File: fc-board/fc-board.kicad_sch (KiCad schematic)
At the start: 11 parts, among them J1 ESQ-125-14-G-D, J2 MSXS-08PFFR-SF7002, J8 M80-5000442

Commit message: Fc board (#9)
* FC board updates

* Finished routing; cleaned library

* Updated RJ45 jack

* Assigned part numbers to everything, replaced ethernet jack

* Finalized layout

* V1 sent for printing
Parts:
- removed J1: ESQ-125-14-G-D, fc-board:ESQ-125-XX-X-D, symbol fc-board:ESQ-125-XX-X-D
- removed J2: MSXS-08PFFR-SF7002, fc-board:MSXS-08PFFR-SF7002, symbol fc-board:MSXS-08PFFR-SF7002
- removed JP14: P1 to GND, Jumper:SolderJumper-2_P1.3mm_Open_Pad1.0x1.5mm, symbol Jumper:SolderJumper_2_Open
- added J1, J3, J4, J5: M80-5000442, fc-board:M80_5000442, symbol fc-board:M80-5000442
- added J10: MTSW-110-13-L-D-1060, fc-board:SAMTEC_BCS-110-L-D-TE, symbol Connector_Generic:Conn_02x10_Odd_Even
- added J11: Conn_Coaxial_Small, Connector_Coaxial:MMCX_Molex_73415-1471_Vertical, symbol Connector:Conn_Coaxial_Small
- added J12: Conn_01x03_Pin, Connector_PinHeader_2.54mm:PinHeader_1x03_P2.54mm_Vertical, symbol Connector:Conn_01x03_Pin
- added J13: 74981104402, fc-board:74981104402, symbol fc-board:74981104402
- added J6: MTSW-104-13-L-D-1060, Connector_PinSocket_2.54mm:PinSocket_2x04_P2.54mm_Vertical, symbol Connector_Generic:Conn_02x04_Counter_Clockwise
- added J7: Conn_02x02_Counter_Clockwise, Connector_PinHeader_2.54mm:PinHeader_2x02_P2.54mm_Vertical, symbol Connector_Generic:Conn_02x02_Counter_Clockwise
- added J8: Conn_01x08_Pin, Connector_PinHeader_2.54mm:PinHeader_2x04_P2.54mm_Vertical, symbol Connector:Conn_01x08_Pin
- added J9: Conn_01x02_Pin, Connector_PinHeader_2.54mm:PinHeader_1x02_P2.54mm_Vertical, symbol Connector:Conn_01x02_Pin
- added JP1: nRPIBOOT, Jumper:SolderJumper-2_P1.3mm_Open_Pad1.0x1.5mm, symbol Jumper:SolderJumper_2_Open
- added JP2: CHASSIS_GND, Jumper:SolderJumper-2_P1.3mm_Open_Pad1.0x1.5mm, symbol Jumper:SolderJumper_2_Open
- added R2, R3: 330, Resistor_SMD:R_1206_3216Metric, symbol Device:R_Small
- added TP1: SDA0, fc-board:TestPoint_THTPad_D2.0mm_Drill1.0mm_JLCrules, symbol Connector:TestPoint
- added TP10: Global_EN, fc-board:TestPoint_THTPad_D2.0mm_Drill1.0mm_JLCrules, symbol Connector:TestPoint
- added TP2: SCL0, fc-board:TestPoint_THTPad_D2.0mm_Drill1.0mm_JLCrules, symbol Connector:TestPoint
- added TP5: +5V, fc-board:TestPoint_THTPad_D2.0mm_Drill1.0mm_JLCrules, symbol Connector:TestPoint
- added TP6: ADS_DRDY, fc-board:TestPoint_THTPad_D2.0mm_Drill1.0mm_JLCrules, symbol Connector:TestPoint
- added TP7: nEXTRST, fc-board:TestPoint_THTPad_D2.0mm_Drill1.0mm_JLCrules, symbol Connector:TestPoint
- added TP8: TestPoint, fc-board:TestPoint_THTPad_D2.0mm_Drill1.0mm_JLCrules, symbol Connector:TestPoint
- added TP9: +3V3, fc-board:TestPoint_THTPad_D2.0mm_Drill1.0mm_JLCrules, symbol Connector:TestPoint
- TP3: value SDA -> SDA1
- TP4: value SCL -> SCL1
- renumbered J8 to J2, R15 to R1
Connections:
- net 3.3V: now also J3.1, J4.1, J5.1, R2.1, R3.1, TP9.1
- net GND: now also J10.15 (Pin_15), J10.16 (Pin_16), J10.17 (Pin_17), J10.18 (Pin_18), J10.19 (Pin_19), J10.20 (Pin_20), J11.2 (Ext), J13.1 (GND), J3.2, J4.2, J5.2, J7.2 (Pin_2), J8.2 (Pin_2), J8.4 (Pin_4), J8.6 (Pin_6), J8.8 (Pin_8), JP1.2 (B), JP2.2 (B)
- net GPIO17: now also J8.1 (Pin_1)
- net GPIO18: now also J8.3 (Pin_3)
- net SCL0: now also J9.2 (Pin_2)
- net SDA0: now also J9.1 (Pin_1)
- net X1+: now also J1.3
- net X1-: now also J1.1
- net X2+: now also J1.4
- net X2-: now also J1.2
- net gpio/nEXTRST: now also TP7.1
- net nRPIBOOT: now also JP1.1 (A)
- net gpio/I2C1_SCL renamed I2C1_SCL
- net I2C1_SCL: now also J4.4
- net gpio/I2C1_SDA renamed I2C1_SDA
- net I2C1_SDA: now also J4.3
- new net: J13.13, R3.2
- new net: J13.11, R2.2
- new net +12V_HEAT: J6.4 (Pin_4)
- new net +15V_BBA: J6.6 (Pin_6)
- new net +5V_BP: J6.2 (Pin_2)
- new net +5V_CM4: J10.13 (Pin_13), J10.14 (Pin_14), J7.1 (Pin_1), TP5.1
- new net +5V_SIPM: J6.8 (Pin_8)
- new net +7.2V_CMT: J6.1 (Pin_1)
- new net -15V_BBA: J6.5 (Pin_5)
- new net -5V_SIPM: J6.3 (Pin_3)
- new net -7.2V_CMT: J6.7 (Pin_7)
- new net BUBBA_TGL: J10.11 (Pin_11), J10.12 (Pin_12)
- new net CHASSIS: J13.S1 (SHIELD1), J13.S2 (SHIELD2), JP2.1 (A)
- new net DET1_TGL: J10.1 (Pin_1), J10.2 (Pin_2)
- new net DET2_TGL: J10.3 (Pin_3), J10.4 (Pin_4)
- new net DET3_TGL: J10.5 (Pin_5), J10.6 (Pin_6)
- new net DET4_TGL: J10.7 (Pin_7), J10.8 (Pin_8)
- new net GPIO19: J8.7 (Pin_7)
- new net GPIO20: J8.5 (Pin_5)
- new net HEATER_TGL: J10.10 (Pin_10), J10.9 (Pin_9)
- new net I2C0_SCL: J3.4, TP2.1
- new net I2C0_SDA: J3.3, TP1.1
- new net PPS: J11.1 (In)
- new net SPI0_CLK: J12.1 (Pin_1)
- new net SPI0_MISO: J12.2 (Pin_2)
- new net SPI0_MOSI: J12.3 (Pin_3)
- new net UART_RX: J5.3
- new net UART_TX: J5.4
- new net USB_N: J7.3 (Pin_3)
- new net USB_P: J7.4 (Pin_4)
- new net Y1+: J13.2 (D1+)
- new net Y1-: J13.3 (D1-)
- new net Y2+: J13.4 (D2+)
- new net Y2-: J13.5 (D2-)
- new net Y3+: J13.6 (D3+)
- new net Y3-: J13.7 (D3-)
- new net Y4+: J13.8 (D4+)
- new net Y4-: J13.9 (D4-)
- new net Y_DUPLEX_LED: J13.14
- new net Y_LINK_LED: J13.12
- new net gpio/Global_EN: TP10.1
- new net i2c-hub/ADS_DRDY: TP6.1
- new net i2c-hub/ADS_RESET: TP8.1
- no-connect marks 10 -> 6
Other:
- removed sheet usb-hub
- sheet gpio ports: added ETH_LEDG, ETH_LEDY1, GPIO19, GPIO20, GPIO21, I2C0_SCL, I2C0_SDA, SPI0_CE0, SPI0_CLK, SPI0_MISO, SPI0_MOSI, UART_RX, UART_TX; removed GPIO10, GPIO14, GPIO15, GPIO4, GPIO7, GPIO8, ID_SC, ID_SD, PELTIER_TGL, SWRI_PWR_IN, UPS_TGL, X3+, X3-, X4+, X4-
- sheet gpio-hispeed ports: added 3.3V, USB_N, USB_P, Y1+, Y1-, Y2+, Y2-, Y3+, Y3-, Y4+, Y4-, Y_DUPLEX_LED, Y_LINK_LED; removed USB2_N, USB2_P, USB_OTG_ID
- sheet i2c-hub ports: added +12V_HEAT, +15V_BBA, +5V_BP, +5V_CM4, +5V_IN, +5V_SIPM, +7V2_CMT, -15V_BBA, -5V_SIPM, -7V2_CMT, ADS_DRDY, ADS_RESET, BIAS_IN, BIAS_REF, BIAS_SCL, BIAS_SDA, RST; removed 15V_BBA, 5V_BP, ??V_SIPM
- sheet spi-hub ports: added 3.3V, CS_LTC2983, INTERRUPT_LTC2983, RESET_LTC2983, SCK, SDI, SDO; removed none
- note added: "3.3 V likely not needed, but included just in case."
- note added: "Bias I2C"
- note added: "CHASSIS!!! CHANGE THIS"
- note added: "CONNECT THESE TO CHASSIS WHEN BOARD REWORKED"
- note added: "Can be repurposed to an additional I2C bus"
- note added: "Debug"
- note added: "General I2C"
- note added: "Gondola ethernet"
- note added: "Interconnect to toggles board"
- note added: "NOT I2C But can be repurposed"
- note added: "Pin 4 is the shield; R1 connects the shield to the FC board GND, which also connects the bias GND to the FC board GND"
- note added: "Pull low to boot from USB"
- note added: "SDA0/SCL0"
- note added: "The LAN7340 schematic shows a ferrite bead connecting GND and CHASSIS"
- note added: "USB"
- note added: "Voltage sensing inputs"
- note removed: "Add another 5 V pin to header?"
- note removed: "Interconnect to power board"
- note removed: "Pin 4 is the shield; R15 connects the shield to the FC board GND, which also connects the bias GND to the FC board GND"
- title: (none) -> Flight Computer Carrier
- moved on the sheet: TP3, TP4

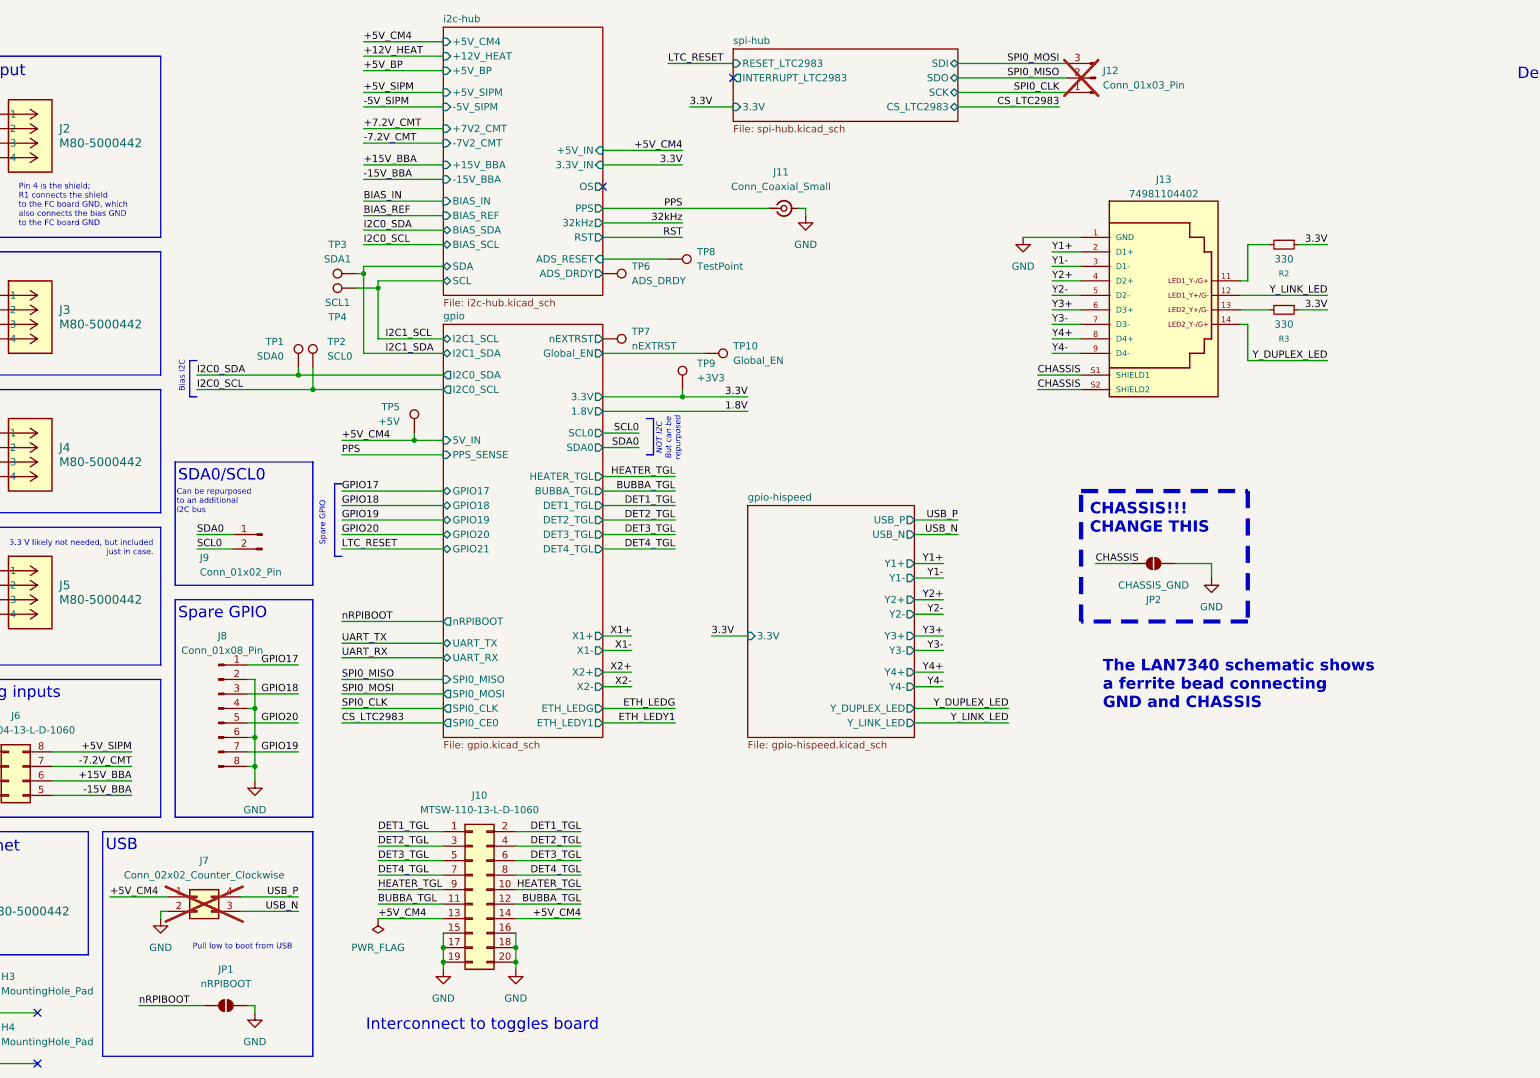
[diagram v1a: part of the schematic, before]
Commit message: Fixed incorrect routes, modified gondola eth, cosmetics
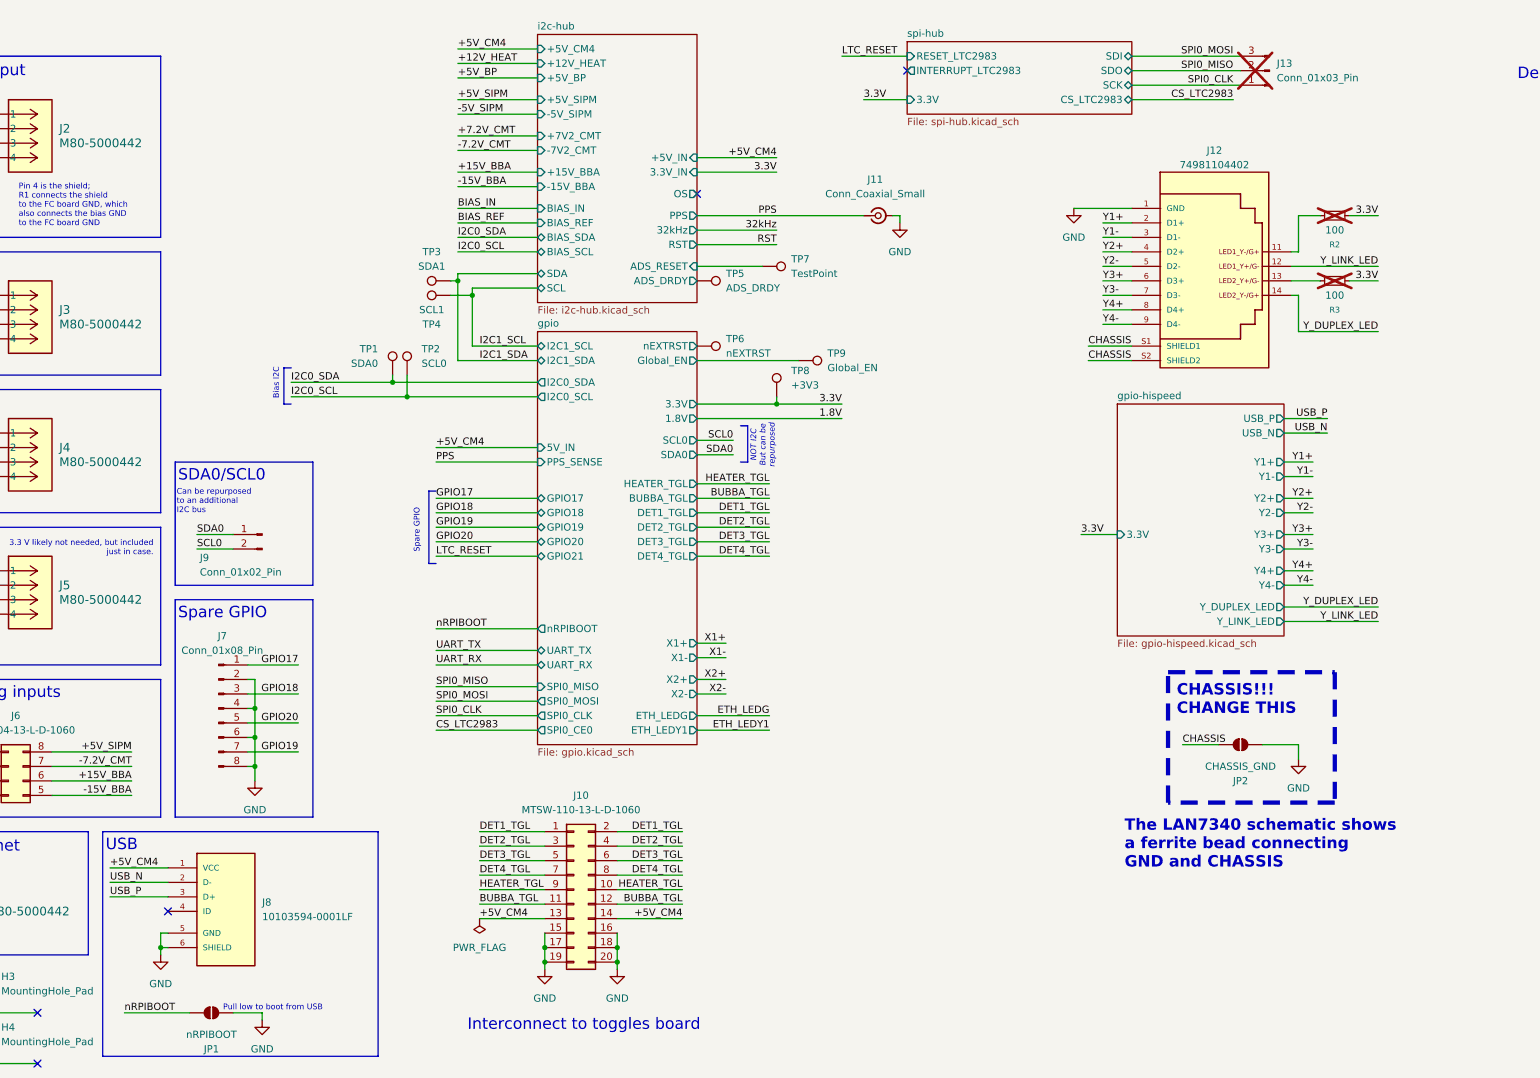
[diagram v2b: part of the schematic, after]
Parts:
- removed J7: Conn_02x02_Counter_Clockwise, Connector_PinHeader_2.54mm:PinHeader_2x02_P2.54mm_Vertical, symbol Connector_Generic:Conn_02x02_Counter_Clockwise
- removed TP5: +5V, fc-board:TestPoint_THTPad_D2.0mm_Drill1.0mm_JLCrules, symbol Connector:TestPoint
- added J8: 10103594-0001LF, fc-board:10103594-0001LF, symbol fc-board:10103594-0001LF
- R2, R3: value 330 -> 100; now not fitted
- renumbered J13 to J12, J12 to J13, J8 to J7, TP6 to TP5, TP7 to TP6, TP8 to TP7, TP9 to TP8, TP10 to TP9
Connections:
- net +5V_CM4: now also J8.1 (VCC)
- net GND: now also J8.5 (GND), J8.6 (SHIELD)
- net USB_N: now also J8.2 (D-)
- net USB_P: now also J8.3 (D+)
- no-connect marks 6 -> 7
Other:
- moved on the sheet: J10, J11, J12, J13, JP1, JP2, TP1, TP2, TP3, TP4, TP5, TP6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

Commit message: Fixed PCIe routing, voltage sensing, added DAQ toggle, LCT interrupt, bias sensing resistors, SD card, and more
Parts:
- removed TP7: TestPoint, fc-board:TestPoint_THTPad_D2.0mm_Drill1.0mm_JLCrules, symbol Connector:TestPoint
- added R2, R3: 5k, Resistor_SMD:R_1206_3216Metric, symbol Device:R_Small
- renumbered R2 to R4, R3 to R5, TP8 to TP7, TP9 to TP8
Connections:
- net GPIO17 is gone; now on net GND: J7.1 (Pin_1)
- net GPIO20 is gone; now on net GND: J7.5 (Pin_5)
- net +5V_BP: now also J6.3 (Pin_3); no longer J6.2 (Pin_2)
- net -5V_SIPM: now also J6.7 (Pin_7); no longer J6.3 (Pin_3)
- net -7.2V_CMT: now also J6.2 (Pin_2); no longer J6.7 (Pin_7)
- net 3.3V: now also R2.2, R3.2
- net GND: no longer J10.19 (Pin_19), J10.20 (Pin_20)
- net I2C0_SCL: now also R2.1
- net I2C0_SDA: now also R3.1
- new net DAQ_TGL: J10.19 (Pin_19), J10.20 (Pin_20)
- no-connect marks 7 -> 6
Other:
- sheet gpio ports: added DAQ_TGL, LTC_INTERRUPT, LTC_RESET; removed GPIO17, GPIO20, GPIO21
- sheet i2c-hub ports: added none; removed ADS_RESET
